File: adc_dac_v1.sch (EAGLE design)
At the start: 100 parts, among them IC1 OPA1662, IC3 ADA4610-2, U1 AD7960BCPZ-RL7, U10 UA78M05CDCYR, U11 LP5907MFX-1.8/NOPB, U12 ADP2300AUJZ-R7, U13 LM317LIPKG3, U14 LM317LIPKG3, U15 LM337LMX/NOPB, U16 ADR395AUJZ-REEL7, U2 AD5453YRMZ-REEL7, U3 ADA4932-1YCPZ-R7, U4 NLSX3018DTR2G, U5 NLSX3018DTR2G, U6 ADS7952SRHBT, U7 Value, U8 REF5025AIDR, U9 ADP150AUJZ-3.3-R7, X1 BU-SMA-G, X2 BU-SMA-G

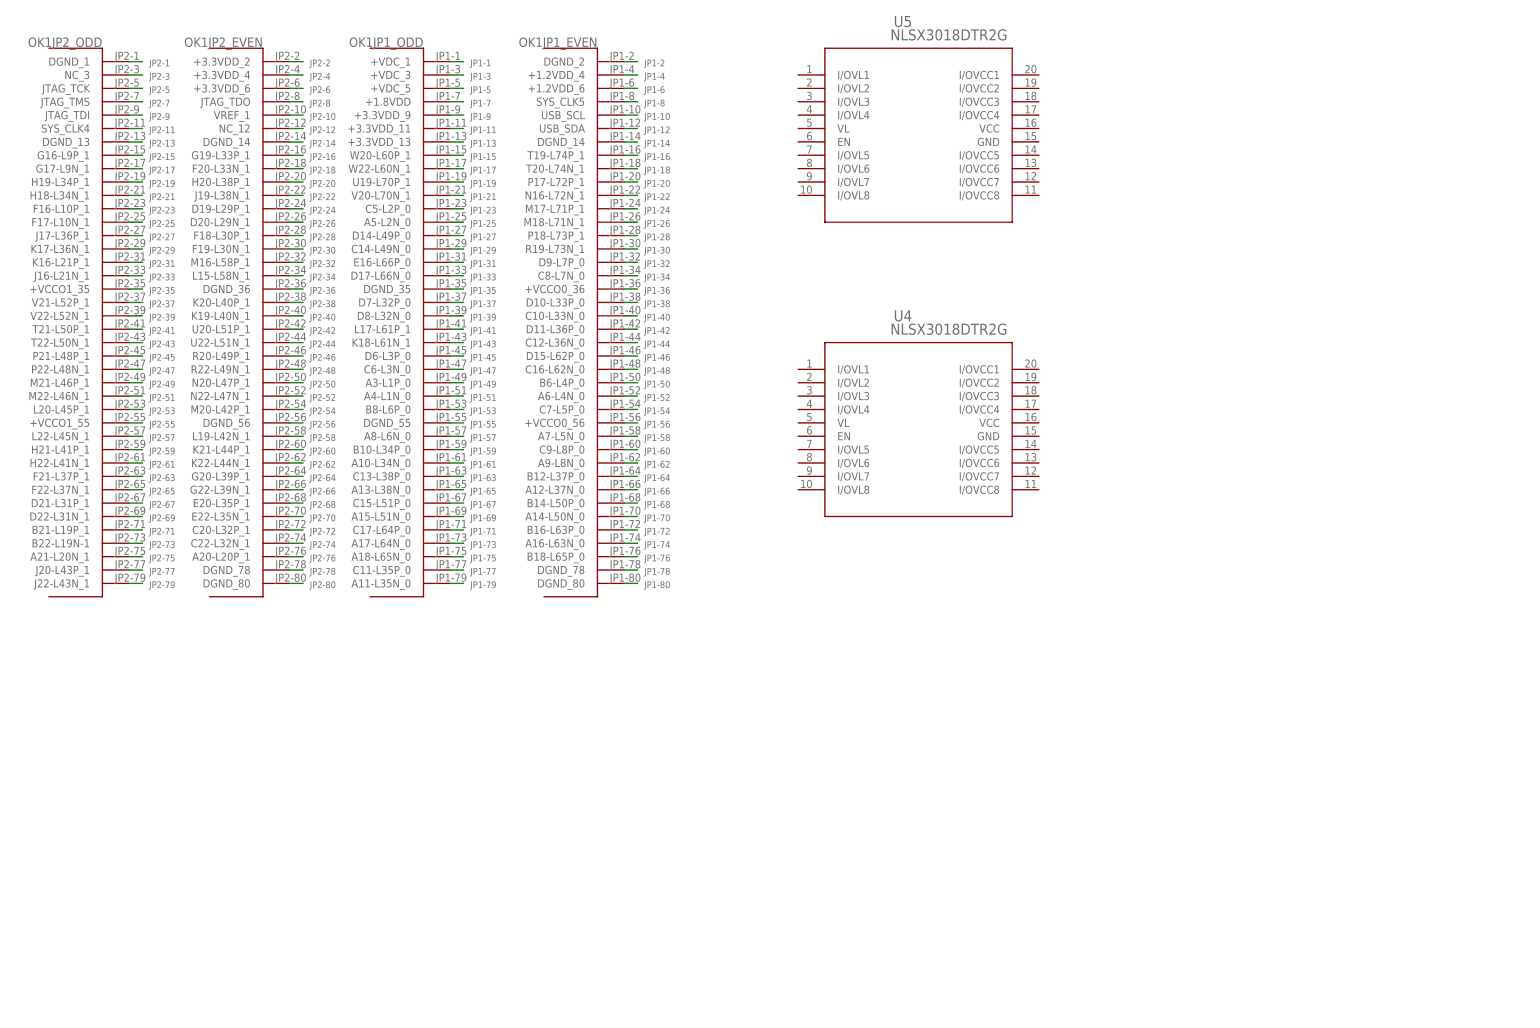
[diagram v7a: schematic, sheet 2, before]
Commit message: updates, modified UltraLibrarian footprint for better name placement
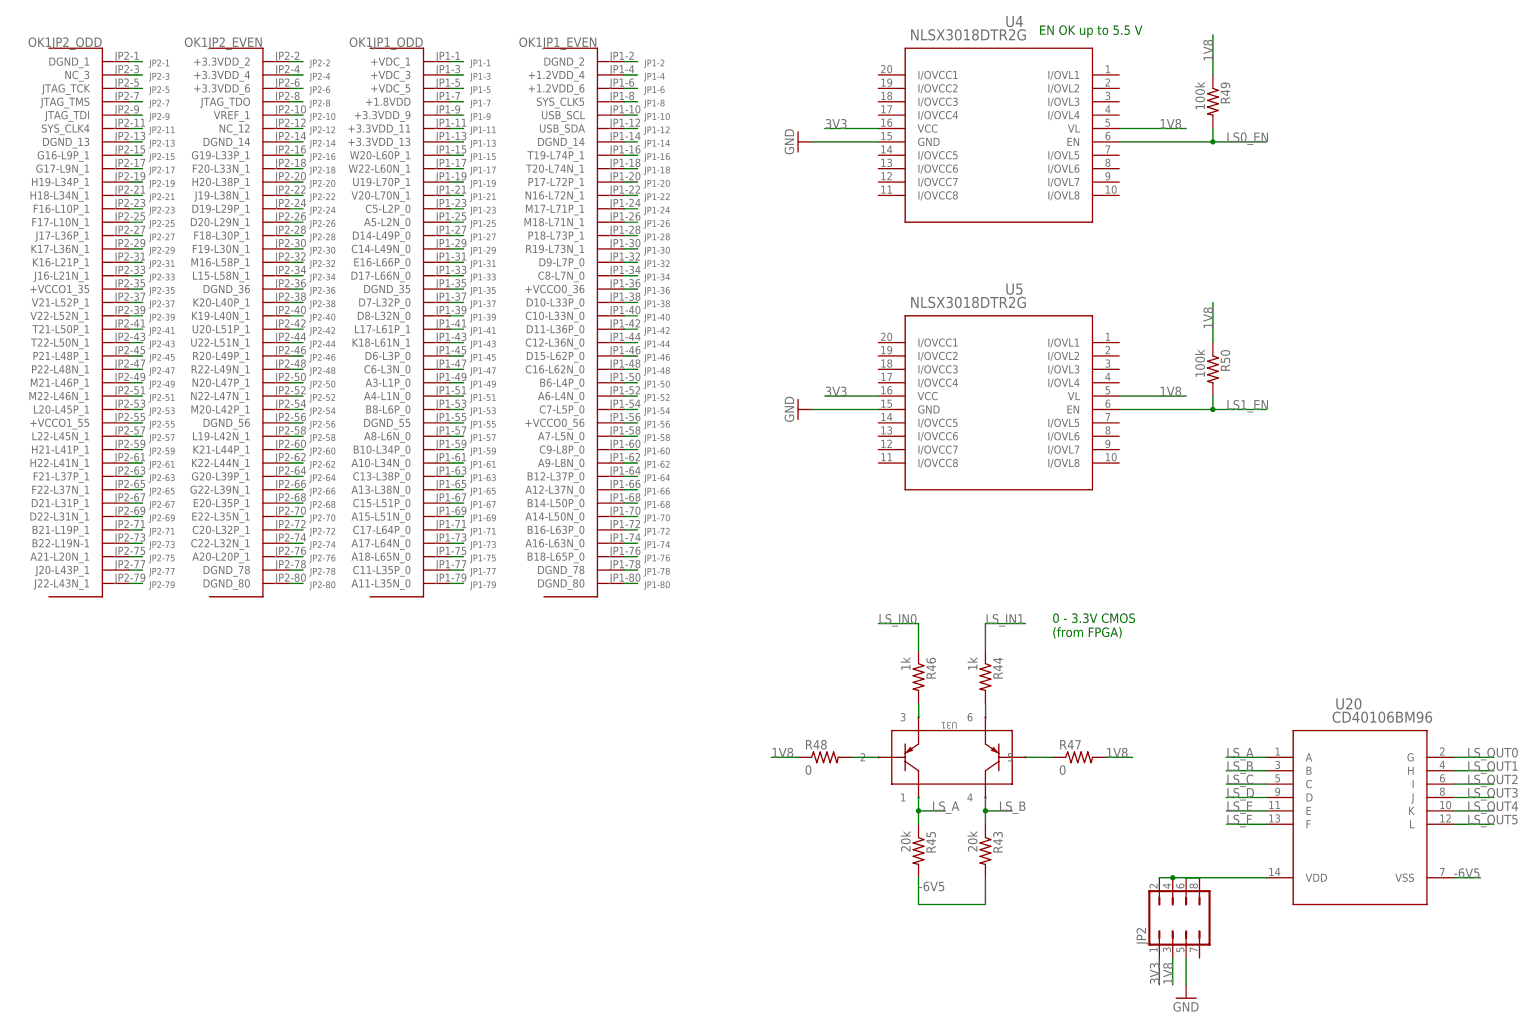
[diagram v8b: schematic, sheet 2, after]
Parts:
- added C45: 10u, rcl:C-USC0603
- added C46, C47, C48, C49, C50: 0.1u, rcl:C-USC0603
- added C51: 1u, rcl:C-USC0603
- added JP2: (no value), jumper:JP4Q
- added R33, R34: 4.7k, rcl:R-US_R0603
- added R35, R36, R49, R50: 100k, rcl:R-US_R0603
- added R41: 240, rcl:R-US_R0603
- added R42, R44, R46: 1k, rcl:R-US_R0603
- added R43, R45: 20k, rcl:R-US_R0603
- added R47, R48: 0, rcl:R-US_R0603
- added U17: MAX5802BAUB+, open_covg:MAX5802BAUB+
- added U18: LM337LMX/NOPB, open_covg:LM337LMX/NOPB
- added U19: MAX6070BAUT21+T, open_covg:MAX6070BAUT21+T
- added U20: CD40106BM96, open_covg:CD40106BM96
- added U31: BC857BS-13-F, open_covg:HN1A01FU-YLFCT
- C25: value 0.1u -> 1u
- U1: device AD7960:AD7960BCPZ-RL7 -> open_covg:AD7960BCPZ-RL7
- U7: value Value -> OPA202
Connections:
- net TR renamed TEMP_REF
- removed net REF: C12.1, C13.1, U1.REF, U1.REF_2, U1.REF_3, U1.REF_4
- new net -6V5: C50.1, R41.1, R43.2, R45.2, U18.OUT, U20.VSS
- new net 2V048_REF: C12.1, C13.1, C46.1, U1.REF, U1.REF_2, U1.REF_3, U1.REF_4, U19.OUTF, U19.OUTS
- new net ADCS_CSB: U6.!CS
- new net ADCS_SDI: U6.SDI
- new net ADCS_SDO: U6.SDO
- new net ADSC_SCLK: U6.SCLK
- new net DACS_0: U17.OUTA
- new net DACS_1: U17.OUTB
- new net DACS_CLRB: R35.1, U17.!CLR
- new net DACS_SCL: R34.1, U17.SCL
- new net DACS_SDA: R33.1, U17.SDA
- new net LS0_EN: R49.2, U4.EN
- new net LS1_EN: R50.2, U5.EN
- new net LS_A: R45.1, U20.A
- new net LS_B: R43.1, U20.B, U31.4
- new net LS_C: U20.C
- new net LS_D: U20.D
- new net LS_E: U20.E
- new net LS_F: U20.F
- new net LS_IN0: R46.1
- new net LS_IN1: R44.1
- new net LS_OUT0: U20.G
- new net LS_OUT1: U20.H
- new net LS_OUT2: U20.I
- new net LS_OUT3: U20.J
- new net LS_OUT4: U20.K
- new net LS_OUT5: U20.L
- new net N$31: R36.2, U17.ADDR
- new net N$34: C47.1, U19.FILTER
- new net N$35: R41.2, R42.1, U18.ADJ
- new net N$37: R48.2, U31.2
- new net N$38: R47.1, U31.5
- new net N$39: R44.2, U31.6
- new net N$40: JP2.2, JP2.4, U20.VDD
- new net N$41: JP2.6, JP2.8
- new net N$43: R46.2, U31.3
- new net N$47: U6.VA+_2
- net 18V_IN: now also C49.1, U18.IN, U18.IN_2, U18.IN_3, U18.IN_4
- net 1V8: now also JP2.3, R47.2, R48.1, R49.1, R50.1, U4.VL, U5.VL
- net 2V5_REF: now also C45.1
- net 3V3: now also JP2.1, R33.2, R34.2, R35.2, U17.VDDIO, U4.VCC, U5.VCC
- net 5V: now also C48.1, C51.1, U17.VDD, U19.EN, U19.IN; no longer U6.VA+_2
- net 5V_REF: now also U17.REF
- net GND: now also C45.2, C46.2, C47.2, C48.2, C49.2, C50.2, C51.2, JP2.5, R36.1, R42.2, U17.GND, U19.GND, U4.GND, U5.GND, U6.EPAD
- net N$29: now also L1.2; no longer L1.1
- net N$6: now also L1.1; no longer L1.2
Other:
- note added: "0 - 3.3V CMOS (from FPGA)"
- note added: "EN OK up to 5.5 V"
- note added: "For FET gate drive (low leakage gate drive)"
- note added: "VA+ analog supply. 5V allows Range 2: VREF*2 VBD+ is digital I/O supply REF from 2V-3V"
- note added: "VREF buffer 9 kOhm VREF input resistance Gain to 10 V (AD5443 max is 12 V) 22 MHz gain-bandwidth"
- note removed: "Need +2.048V ref here"
- note removed: "VA+ analog supply. 5V allows Range 2: VREF*2 VBD+ is digital I/O supply"
- note removed: "VREF buffer 9 kOhm VREF input resistance Gain to 10 V (AD5443 max is 12 V)"
- moved on the sheet: C1, C2, C21, L1, U4, U5
